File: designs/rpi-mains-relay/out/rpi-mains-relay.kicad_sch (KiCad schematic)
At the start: 0 parts

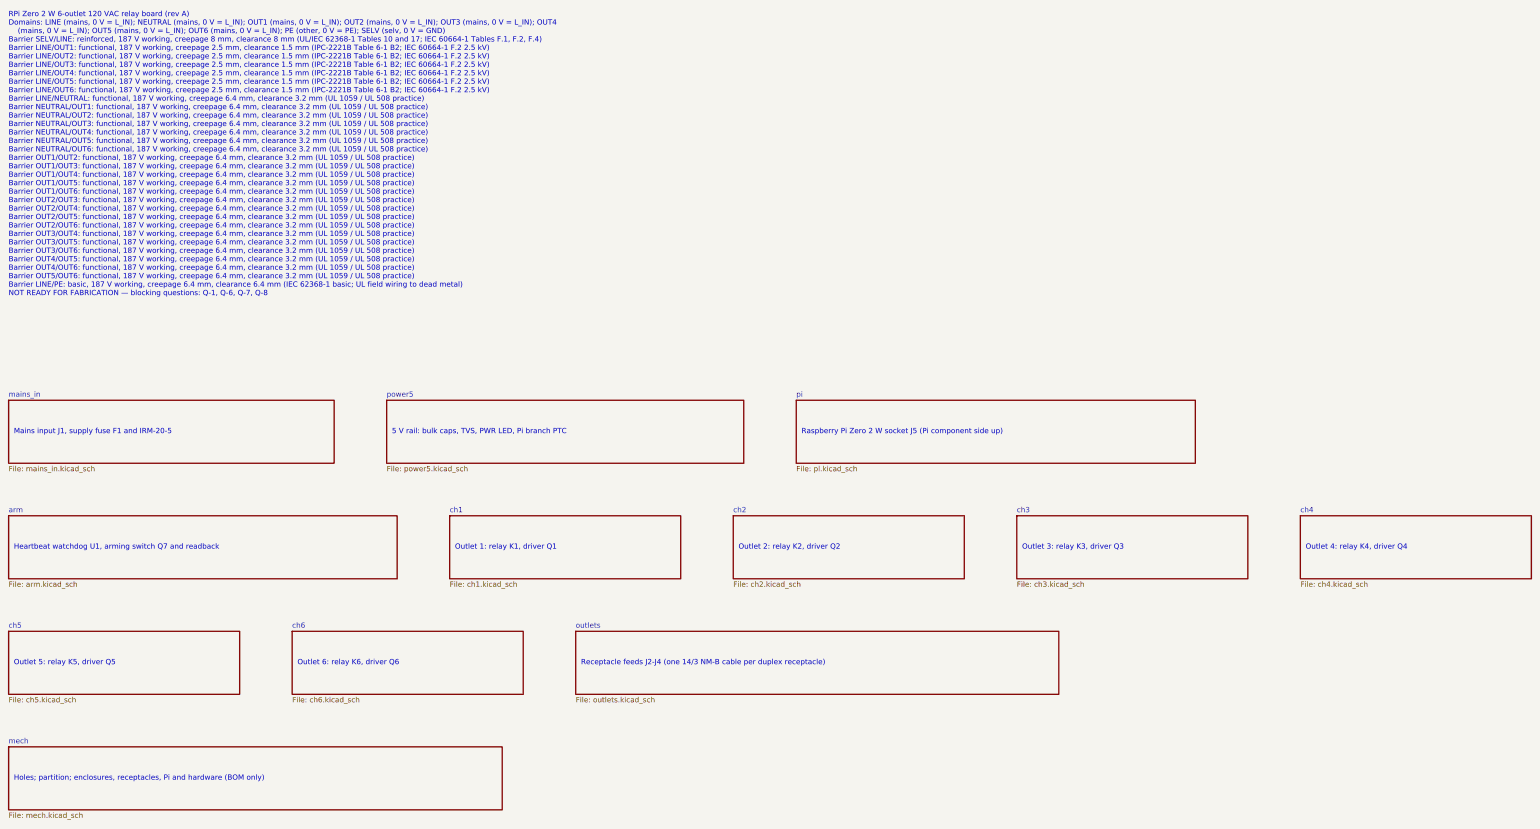
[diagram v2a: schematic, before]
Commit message: designs/rpi-mains-relay: revision 3 — one enclosure (user decision)
User chose one enclosure (2026-10-23, Q-8). An ABB/Carlon NS14126 polycarbonate UL 50
Type 4X enclosure (14 x 12 x 6 in; Wi-Fi passes) holds the unchanged 200 x 150 mm board on
its back panel; three split-tab TR duplex receptacles mount in a 3-gang cut-out in the
cover on a 6.4 mm polycarbonate subplate, yokes bonded by pigtails, 14 AWG leads with a
service loop to J2-J4. A partition keeps receptacles and field wiring away from the board's
SELV side; the Pi is >= 150 mm from them. 15.5 W gives 49 C inside at a 40 C room.

No listed nonmetallic enclosure with receptacle openings in its cover was found, so
cover-mounted receptacles need a field evaluation or a UL 508A shop: new blocking Q-17.
All mains barriers ac=True. Build: 0 errors, 0 warnings, 31 waived, ERC clean, netlist
identical (L_IN now correctly flagged: relays sit on the wire side of the supply fuse;
the branch-breaker waiver covers it).

Co-Authored-By: Claude Opus 5.5 <noreply@anthropic.com>
Claude-Session: https://claude.ai/code/session_01VFJn9VbX8h27kf4LpLwEtn
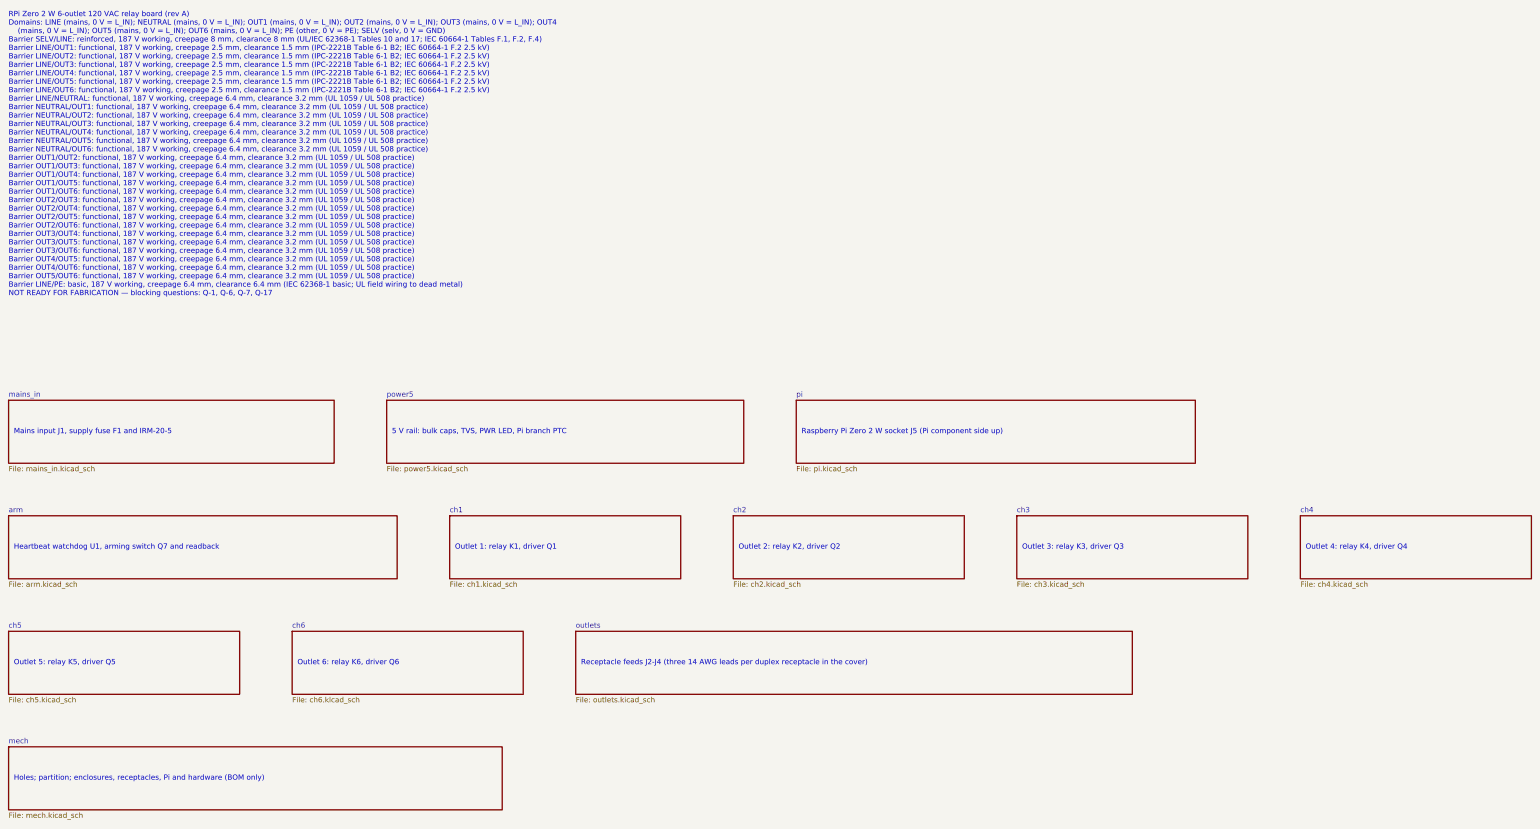
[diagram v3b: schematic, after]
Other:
- note added: "Receptacle feeds J2-J4 (three 14 AWG leads per duplex receptacle in the cover)"
- note removed: "Receptacle feeds J2-J4 (one 14/3 NM-B cable per duplex receptacle)"
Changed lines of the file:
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@@
 	(sheet
 		(at 162.56 175.26)
-		(size 116.84 15.24)
+		(size 134.62 15.24)
 		(exclude_from_sim no)
 		(in_bom yes)
@@
 		)
 	)
-	(text "Receptacle feeds J2-J4 (one 14/3 NM-B cable per duplex receptacle)"
+	(text "Receptacle feeds J2-J4 (three 14 AWG leads per duplex receptacle in the cover)"
 		(exclude_from_sim no)
 		(at 163.83 182.88 0)
@@
 		)
 	)
-	(text "RPi Zero 2 W 6-outlet 120 VAC relay board (rev A)\nDomains: LINE (mains, 0 V = L_IN); NEUTRAL (mains, 0 V = L_IN); OUT1 (mains, 0 V = L_IN); OUT2 (mains, 0 V = L_IN); OUT3 (mains, 0 V = L_IN); OUT4\n    (mains, 0 V = L_IN); OUT5 (mains, 0 V = L_IN); OUT6 (mains, 0 V = L_IN); PE (other, 0 V = PE); SELV (selv, 0 V = GND)\nBarrier SELV/LINE: reinforced, 187 V working, creepage 8 mm, clearance 8 mm (UL/IEC 62368-1 Tables 10 and 17; IEC 60664-1 Tables F.1, F.2, F.4)\nBarrier LINE/OUT1: functional, 187 V working, creepage 2.5 mm, clearance 1.5 mm (IPC-2221B Table 6-1 B2; IEC 60664-1 F.2 2.5 kV)\nBarrier LINE/OUT2: functional, 187 V working, creepage 2.5 mm, clearance 1.5 mm (IPC-2221B Table 6-1 B2; IEC 60664-1 F.2 2.5 kV)\nBarrier LINE/OUT3: functional, 187 V working, creepage 2.5 mm, clearance 1.5 mm (IPC-2221B Table 6-1 B2; IEC 60664-1 F.2 2.5 kV)\nBarrier LINE/OUT4: functional, 187 V working, creepage 2.5 mm, clearance 1.5 mm (IPC-2221B Table 6-1 B2; IEC 60664-1 F.2 2.5 kV)\nBarrier LINE/OUT5: functional, 187 V working, creepage 2.5 mm, clearance 1.5 mm (IPC-2221B Table 6-1 B2; IEC 60664-1 F.2 2.5 kV)\nBarrier LINE/OUT6: functional, 187 V working, creepage 2.5 mm, clearance 1.5 mm (IPC-2221B Table 6-1 B2; IEC 60664-1 F.2 2.5 kV)\nBarrier LINE/NEUTRAL: functional, 187 V working, creepage 6.4 mm, clearance 3.2 mm (UL 1059 / UL 508 practice)\nBarrier NEUTRAL/OUT1: functional, 187 V working, creepage 6.4 mm, clearance 3.2 mm (UL 1059 / UL 508 practice)\nBarrier NEUTRAL/OUT2: functional, 187 V working, creepage 6.4 mm, clearance 3.2 mm (UL 1059 / UL 508 practice)\nBarrier NEUTRAL/OUT3: functional, 187 V working, creepage 6.4 mm, clearance 3.2 mm (UL 1059 / UL 508 practice)\nBarrier NEUTRAL/OUT4: functional, 187 V working, creepage 6.4 mm, clearance 3.2 mm (UL 1059 / UL 508 practice)\nBarrier NEUTRAL/OUT5: functional, 187 V working, creepage 6.4 mm, clearance 3.2 mm (UL 1059 / UL 508 practice)\nBarrier NEUTRAL/OUT6: functional, 187 V working, creepage 6.4 mm, clearance 3.2 mm (UL 1059 / UL 508 practice)\nBarrier OUT1/OUT2: functional, 187 V working, creepage 6.4 mm, clearance 3.2 mm (UL 1059 / UL 508 practice)\nBarrier OUT1/OUT3: functional, 187 V working, creepage 6.4 mm, clearance 3.2 mm (UL 1059 / UL 508 practice)\nBarrier OUT1/OUT4: functional, 187 V working, creepage 6.4 mm, clearance 3.2 mm (UL 1059 / UL 508 practice)\nBarrier OUT1/OUT5: functional, 187 V working, creepage 6.4 mm, clearance 3.2 mm (UL 1059 / UL 508 practice)\nBarrier OUT1/OUT6: functional, 187 V working, creepage 6.4 mm, clearance 3.2 mm (UL 1059 / UL 508 practice)\nBarrier OUT2/OUT3: functional, 187 V working, creepage 6.4 mm, clearance 3.2 mm (UL 1059 / UL 508 practice)\nBarrier OUT2/OUT4: functional, 187 V working, creepage 6.4 mm, clearance 3.2 mm (UL 1059 / UL 508 practice)\nBarrier OUT2/OUT5: functional, 187 V working, creepage 6.4 mm, clearance 3.2 mm (UL 1059 / UL 508 practice)\nBarrier OUT2/OUT6: functional, 187 V working, creepage 6.4 mm, clearance 3.2 mm (UL 1059 / UL 508 practice)\nBarrier OUT3/OUT4: functional, 187 V working, creepage 6.4 mm, clearance 3.2 mm (UL 1059 / UL 508 practice)\nBarrier OUT3/OUT5: functional, 187 V working, creepage 6.4 mm, clearance 3.2 mm (UL 1059 / UL 508 practice)\nBarrier OUT3/OUT6: functional, 187 V working, creepage 6.4 mm, clearance 3.2 mm (UL 1059 / UL 508 practice)\nBarrier OUT4/OUT5: functional, 187 V working, creepage 6.4 mm, clearance 3.2 mm (UL 1059 / UL 508 practice)\nBarrier OUT4/OUT6: functional, 187 V working, creepage 6.4 mm, clearance 3.2 mm (UL 1059 / UL 508 practice)\nBarrier OUT5/OUT6: functional, 187 V working, creepage 6.4 mm, clearance 3.2 mm (UL 1059 / UL 508 practice)\nBarrier LINE/PE: basic, 187 V working, creepage 6.4 mm, clearance 6.4 mm (IEC 62368-1 basic; UL field wiring to dead metal)\nNOT READY FOR FABRICATION — blocking questions: Q-1, Q-6, Q-7, Q-8"
+	(text "RPi Zero 2 W 6-outlet 120 VAC relay board (rev A)\nDomains: LINE (mains, 0 V = L_IN); NEUTRAL (mains, 0 V = L_IN); OUT1 (mains, 0 V = L_IN); OUT2 (mains, 0 V = L_IN); OUT3 (mains, 0 V = L_IN); OUT4\n    (mains, 0 V = L_IN); OUT5 (mains, 0 V = L_IN); OUT6 (mains, 0 V = L_IN); PE (other, 0 V = PE); SELV (selv, 0 V = GND)\nBarrier SELV/LINE: reinforced, 187 V working, creepage 8 mm, clearance 8 mm (UL/IEC 62368-1 Tables 10 and 17; IEC 60664-1 Tables F.1, F.2, F.4)\nBarrier LINE/OUT1: functional, 187 V working, creepage 2.5 mm, clearance 1.5 mm (IPC-2221B Table 6-1 B2; IEC 60664-1 F.2 2.5 kV)\nBarrier LINE/OUT2: functional, 187 V working, creepage 2.5 mm, clearance 1.5 mm (IPC-2221B Table 6-1 B2; IEC 60664-1 F.2 2.5 kV)\nBarrier LINE/OUT3: functional, 187 V working, creepage 2.5 mm, clearance 1.5 mm (IPC-2221B Table 6-1 B2; IEC 60664-1 F.2 2.5 kV)\nBarrier LINE/OUT4: functional, 187 V working, creepage 2.5 mm, clearance 1.5 mm (IPC-2221B Table 6-1 B2; IEC 60664-1 F.2 2.5 kV)\nBarrier LINE/OUT5: functional, 187 V working, creepage 2.5 mm, clearance 1.5 mm (IPC-2221B Table 6-1 B2; IEC 60664-1 F.2 2.5 kV)\nBarrier LINE/OUT6: functional, 187 V working, creepage 2.5 mm, clearance 1.5 mm (IPC-2221B Table 6-1 B2; IEC 60664-1 F.2 2.5 kV)\nBarrier LINE/NEUTRAL: functional, 187 V working, creepage 6.4 mm, clearance 3.2 mm (UL 1059 / UL 508 practice)\nBarrier NEUTRAL/OUT1: functional, 187 V working, creepage 6.4 mm, clearance 3.2 mm (UL 1059 / UL 508 practice)\nBarrier NEUTRAL/OUT2: functional, 187 V working, creepage 6.4 mm, clearance 3.2 mm (UL 1059 / UL 508 practice)\nBarrier NEUTRAL/OUT3: functional, 187 V working, creepage 6.4 mm, clearance 3.2 mm (UL 1059 / UL 508 practice)\nBarrier NEUTRAL/OUT4: functional, 187 V working, creepage 6.4 mm, clearance 3.2 mm (UL 1059 / UL 508 practice)\nBarrier NEUTRAL/OUT5: functional, 187 V working, creepage 6.4 mm, clearance 3.2 mm (UL 1059 / UL 508 practice)\nBarrier NEUTRAL/OUT6: functional, 187 V working, creepage 6.4 mm, clearance 3.2 mm (UL 1059 / UL 508 practice)\nBarrier OUT1/OUT2: functional, 187 V working, creepage 6.4 mm, clearance 3.2 mm (UL 1059 / UL 508 practice)\nBarrier OUT1/OUT3: functional, 187 V working, creepage 6.4 mm, clearance 3.2 mm (UL 1059 / UL 508 practice)\nBarrier OUT1/OUT4: functional, 187 V working, creepage 6.4 mm, clearance 3.2 mm (UL 1059 / UL 508 practice)\nBarrier OUT1/OUT5: functional, 187 V working, creepage 6.4 mm, clearance 3.2 mm (UL 1059 / UL 508 practice)\nBarrier OUT1/OUT6: functional, 187 V working, creepage 6.4 mm, clearance 3.2 mm (UL 1059 / UL 508 practice)\nBarrier OUT2/OUT3: functional, 187 V working, creepage 6.4 mm, clearance 3.2 mm (UL 1059 / UL 508 practice)\nBarrier OUT2/OUT4: functional, 187 V working, creepage 6.4 mm, clearance 3.2 mm (UL 1059 / UL 508 practice)\nBarrier OUT2/OUT5: functional, 187 V working, creepage 6.4 mm, clearance 3.2 mm (UL 1059 / UL 508 practice)\nBarrier OUT2/OUT6: functional, 187 V working, creepage 6.4 mm, clearance 3.2 mm (UL 1059 / UL 508 practice)\nBarrier OUT3/OUT4: functional, 187 V working, creepage 6.4 mm, clearance 3.2 mm (UL 1059 / UL 508 practice)\nBarrier OUT3/OUT5: functional, 187 V working, creepage 6.4 mm, clearance 3.2 mm (UL 1059 / UL 508 practice)\nBarrier OUT3/OUT6: functional, 187 V working, creepage 6.4 mm, clearance 3.2 mm (UL 1059 / UL 508 practice)\nBarrier OUT4/OUT5: functional, 187 V working, creepage 6.4 mm, clearance 3.2 mm (UL 1059 / UL 508 practice)\nBarrier OUT4/OUT6: functional, 187 V working, creepage 6.4 mm, clearance 3.2 mm (UL 1059 / UL 508 practice)\nBarrier OUT5/OUT6: functional, 187 V working, creepage 6.4 mm, clearance 3.2 mm (UL 1059 / UL 508 practice)\nBarrier LINE/PE: basic, 187 V working, creepage 6.4 mm, clearance 6.4 mm (IEC 62368-1 basic; UL field wiring to dead metal)\nNOT READY FOR FABRICATION — blocking questions: Q-1, Q-6, Q-7, Q-17"
 		(exclude_from_sim no)
 		(at 25.4 25.4 0)
